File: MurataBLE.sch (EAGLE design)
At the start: 50 parts, among them CON1 C-2235, IC1 I-5448, IC3 74LVC1G00DBV, IC4 IC_MEMORY_8P_AT25XE011_SOP, IC5 IC_MEMORY_8P_AT25XE011_TSSOP, Q1 FC-135 32.7680KA-AG3, U1 LBCA2HNZYZ-711, X1 C-04397

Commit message: [ USB ] r0.4
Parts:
- added ICON1: r0.4, mylib:ICON_REVISION_1.2
- TR1: device mylib:TR_PMOS_GDS_SOT23 -> mylib:PMOS_BSS84_SOT23
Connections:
- net N$14 renamed P1_15
- net N$25 renamed P0_32
- net N$26 renamed P0_16
- net N$27 renamed P0_15
- net P0_2: now also IC2.P0_7/CTS
- net P0_3: now also IC2.P0_8/MISO0
- net P0_6: now also IC2.P0_9/MOSI0
- net P1_1: now also IC2.P0_21/MOSI1
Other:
- note removed: "rev 0.3"
- moved on the sheet: TP1, TP2, TP3, TP4, TP5, TP6, TP7, TP8
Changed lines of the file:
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@@
 <part name="SUPPLY14" library="mylib" deviceset="GND" device=""/>
 <part name="SUPPLY15" library="mylib" deviceset="GND" device=""/>
-<part name="TR1" library="mylib" deviceset="TR_PMOS_GDS" device="_SOT23" value="I-4269"/>
+<part name="TR1" library="mylib" deviceset="PMOS_*" device="_SOT23" technology="BSS84" value="I-4269"/>
 <part name="R10" library="mylib" deviceset="R_US_*" device="_1005" technology="1.5K" value="1.5k/1005"/>
 <part name="IC3" library="74xx-little-us_local" deviceset="74*1G00" device="DBV" technology="LVC" value="74LVC1G00DBV"/>
@@
 <part name="C11" library="mylib" deviceset="C_SMD_*" device="_1005" technology="0.1U" value="0.1u/1005"/>
 <part name="C12" library="mylib" deviceset="C_SMD_*" device="_1005" technology="0.1U" value="0.1u/1005"/>
+<part name="ICON1" library="mylib" deviceset="ICON_REVISION" device="_1.2" value="r0.4"/>
 </parts>
 <sheets>
 <sheet>
 <plain>
-<text x="162.56" y="5.08" size="5.08" layer="94">rev 0.3</text>
 <text x="190.5" y="96.52" size="1.778" layer="91">Vf@5mA:
 (R) = 1.9V
 (G) = 2.9V
 (B) = 2.8V</text>
-<text x="187.96" y="50.8" size="1.778" layer="94">TGT_TX &lt;- P0_0
+<text x="203.2" y="50.8" size="1.778" layer="94">TGT_TX &lt;- P0_0
 TGT_RX -&gt; P0_1</text>
 <text x="233.68" y="139.7" size="1.778" layer="94">P0_0 -&gt; TGT_TX
@@
 <instance part="LED1" gate="G" x="175.26" y="96.52" rot="R90"/>
 <instance part="LED1" gate="B" x="180.34" y="93.98" rot="R90"/>
-<instance part="TP5" gate="G$1" x="165.1" y="55.88"/>
-<instance part="TP6" gate="G$1" x="165.1" y="48.26" rot="R180"/>
-<instance part="TP7" gate="G$1" x="185.42" y="48.26" rot="R180"/>
-<instance part="TP8" gate="G$1" x="185.42" y="55.88"/>
+<instance part="TP5" gate="G$1" x="180.34" y="55.88"/>
+<instance part="TP6" gate="G$1" x="180.34" y="48.26" rot="R180"/>
+<instance part="TP7" gate="G$1" x="200.66" y="48.26" rot="R180"/>
+<instance part="TP8" gate="G$1" x="200.66" y="55.88"/>
 <instance part="X1" gate="-1" x="231.14" y="93.98" rot="MR0"/>
 <instance part="X1" gate="-2" x="231.14" y="91.44" rot="MR0"/>
@@
 <instance part="X1" gate="-13" x="231.14" y="63.5" rot="MR0"/>
 <instance part="X1" gate="-14" x="231.14" y="60.96" rot="MR0"/>
-<instance part="TP1" gate="1" x="167.64" y="53.34"/>
-<instance part="TP2" gate="1" x="167.64" y="50.8"/>
-<instance part="TP3" gate="1" x="182.88" y="53.34" rot="R180"/>
-<instance part="TP4" gate="1" x="182.88" y="50.8" rot="R180"/>
+<instance part="TP1" gate="1" x="182.88" y="53.34"/>
+<instance part="TP2" gate="1" x="182.88" y="50.8"/>
+<instance part="TP3" gate="1" x="198.12" y="53.34" rot="R180"/>
+<instance part="TP4" gate="1" x="198.12" y="50.8" rot="R180"/>
 <instance part="TP9" gate="1" x="144.78" y="15.24" rot="R90"/>
 <instance part="TP10" gate="1" x="149.86" y="15.24" rot="R90"/>
@@
 <instance part="C11" gate="G$1" x="48.26" y="68.58"/>
 <instance part="C12" gate="G$1" x="48.26" y="45.72"/>
+<instance part="ICON1" gate="G$1" x="162.56" y="5.08"/>
 </instances>
 <busses>
@@
 <label x="10.16" y="40.64" size="1.778" layer="95"/>
 </segment>
+<segment>
+<wire x1="170.18" y1="83.82" x2="157.48" y2="83.82" width="0.1524" layer="91"/>
+<pinref part="IC2" gate="G$1" pin="P0_9/MOSI0"/>
+<label x="170.18" y="83.82" size="1.778" layer="95"/>
+</segment>
 </net>
 <net name="P0_7" class="0">
@@
 <label x="48.26" y="35.56" size="1.778" layer="95"/>
 </segment>
+<segment>
+<wire x1="170.18" y1="88.9" x2="157.48" y2="88.9" width="0.1524" layer="91"/>
+<pinref part="IC2" gate="G$1" pin="P0_7/CTS"/>
+<label x="170.18" y="88.9" size="1.778" layer="95"/>
+</segment>
 </net>
 <net name="P0_3" class="0">
@@
 <label x="10.16" y="38.1" size="1.778" layer="95"/>
 </segment>
+<segment>
+<wire x1="170.18" y1="86.36" x2="157.48" y2="86.36" width="0.1524" layer="91"/>
+<pinref part="IC2" gate="G$1" pin="P0_8/MISO0"/>
+<label x="170.18" y="86.36" size="1.778" layer="95"/>
+</segment>
 </net>
 <net name="P0_4" class="0">
@@
 <pinref part="IC5" gate="G$1" pin="!CS"/>
 <label x="10.16" y="43.18" size="1.778" layer="95"/>
+</segment>
+<segment>
+<wire x1="170.18" y1="91.44" x2="157.48" y2="91.44" width="0.1524" layer="91"/>
+<pinref part="IC2" gate="G$1" pin="P0_21/MOSI1"/>
+<label x="170.18" y="91.44" size="1.778" layer="95"/>
 </segment>
 </net>
@@
 <segment>
 <pinref part="TP5" gate="G$1" pin="TP"/>
-<junction x="165.1" y="53.34"/>
+<junction x="180.34" y="53.34"/>
 <pinref part="TP1" gate="1" pin="1"/>
-<wire x1="193.04" y1="53.34" x2="185.42" y2="53.34" width="0.1524" layer="91"/>
+<wire x1="208.28" y1="53.34" x2="200.66" y2="53.34" width="0.1524" layer="91"/>
 <pinref part="TP8" gate="G$1" pin="TP"/>
-<junction x="185.42" y="53.34"/>
+<junction x="200.66" y="53.34"/>
 <pinref part="TP3" gate="1" pin="1"/>
-<wire x1="165.1" y1="53.34" x2="167.64" y2="55.88" width="0.1524" layer="91"/>
-<wire x1="167.64" y1="55.88" x2="182.88" y2="55.88" width="0.1524" layer="91"/>
-<wire x1="182.88" y1="55.88" x2="185.42" y2="53.34" width="0.1524" layer="91"/>
-<wire x1="157.48" y1="53.34" x2="165.1" y2="53.34" width="0.1524" layer="91"/>
+<wire x1="180.34" y1="53.34" x2="182.88" y2="55.88" width="0.1524" layer="91"/>
+<wire x1="182.88" y1="55.88" x2="198.12" y2="55.88" width="0.1524" layer="91"/>
+<wire x1="198.12" y1="55.88" x2="200.66" y2="53.34" width="0.1524" layer="91"/>
+<wire x1="157.48" y1="53.34" x2="180.34" y2="53.34" width="0.1524" layer="91"/>
 <pinref part="IC2" gate="G$1" pin="P0_18/RXD&lt;-"/>
 </segment>
@@
 <net name="TGT_RX" class="0">
 <segment>
-<wire x1="193.04" y1="50.8" x2="185.42" y2="50.8" width="0.1524" layer="91"/>
+<wire x1="208.28" y1="50.8" x2="200.66" y2="50.8" width="0.1524" layer="91"/>
 <pinref part="TP7" gate="G$1" pin="TP"/>
-<junction x="185.42" y="50.8"/>
+<junction x="200.66" y="50.8"/>
 <pinref part="TP4" gate="1" pin="1"/>
 <pinref part="TP6" gate="G$1" pin="TP"/>
-<junction x="165.1" y="50.8"/>
+<junction x="180.34" y="50.8"/>
 <pinref part="TP2" gate="1" pin="1"/>
-<wire x1="185.42" y1="50.8" x2="182.88" y2="48.26" width="0.1524" layer="91"/>
-<wire x1="182.88" y1="48.26" x2="167.64" y2="48.26" width="0.1524" layer="91"/>
-<wire x1="167.64" y1="48.26" x2="165.1" y2="50.8" width="0.1524" layer="91"/>
-<wire x1="157.48" y1="50.8" x2="165.1" y2="50.8" width="0.1524" layer="91"/>
+<wire x1="200.66" y1="50.8" x2="198.12" y2="48.26" width="0.1524" layer="91"/>
+<wire x1="198.12" y1="48.26" x2="182.88" y2="48.26" width="0.1524" layer="91"/>
+<wire x1="182.88" y1="48.26" x2="180.34" y2="50.8" width="0.1524" layer="91"/>
+<wire x1="157.48" y1="50.8" x2="180.34" y2="50.8" width="0.1524" layer="91"/>
 <pinref part="IC2" gate="G$1" pin="P0_19/TXD-&gt;"/>
 </segment>
@@
 </segment>
 </net>
-<net name="N$14" class="0">
+<net name="P1_15" class="0">
 <segment>
 <pinref part="IC2" gate="G$1" pin="P1_15"/>
 <wire x1="157.48" y1="58.42" x2="162.56" y2="58.42" width="0.1524" layer="91"/>
+<label x="162.56" y="58.42" size="1.778" layer="95"/>
 </segment>
 <segment>
@@
 </segment>
 </net>
-<net name="N$25" class="0">
+<net name="P0_32" class="0">
 <segment>
 <pinref part="IC2" gate="G$1" pin="P0_32/AD7"/>
 <wire x1="157.48" y1="60.96" x2="162.56" y2="60.96" width="0.1524" layer="91"/>
+<label x="162.56" y="60.96" size="1.778" layer="95"/>
 </segment>
 <segment>
@@
 </segment>
 </net>
-<net name="N$26" class="0">
+<net name="P0_16" class="0">
 <segment>
 <pinref part="IC2" gate="G$1" pin="P0_16/AD5"/>
 <wire x1="157.48" y1="63.5" x2="162.56" y2="63.5" width="0.1524" layer="91"/>
+<label x="162.56" y="63.5" size="1.778" layer="95"/>
 </segment>
 <segment>
@@
 </segment>
 </net>
-<net name="N$27" class="0">
+<net name="P0_15" class="0">
 <segment>
 <pinref part="IC2" gate="G$1" pin="P0_15/SWDIO/AD4"/>
 <wire x1="157.48" y1="66.04" x2="162.56" y2="66.04" width="0.1524" layer="91"/>
-</segment>
-<segment>
+<label x="162.56" y="66.04" size="1.778" layer="95"/>
+</segment>
+<segment>

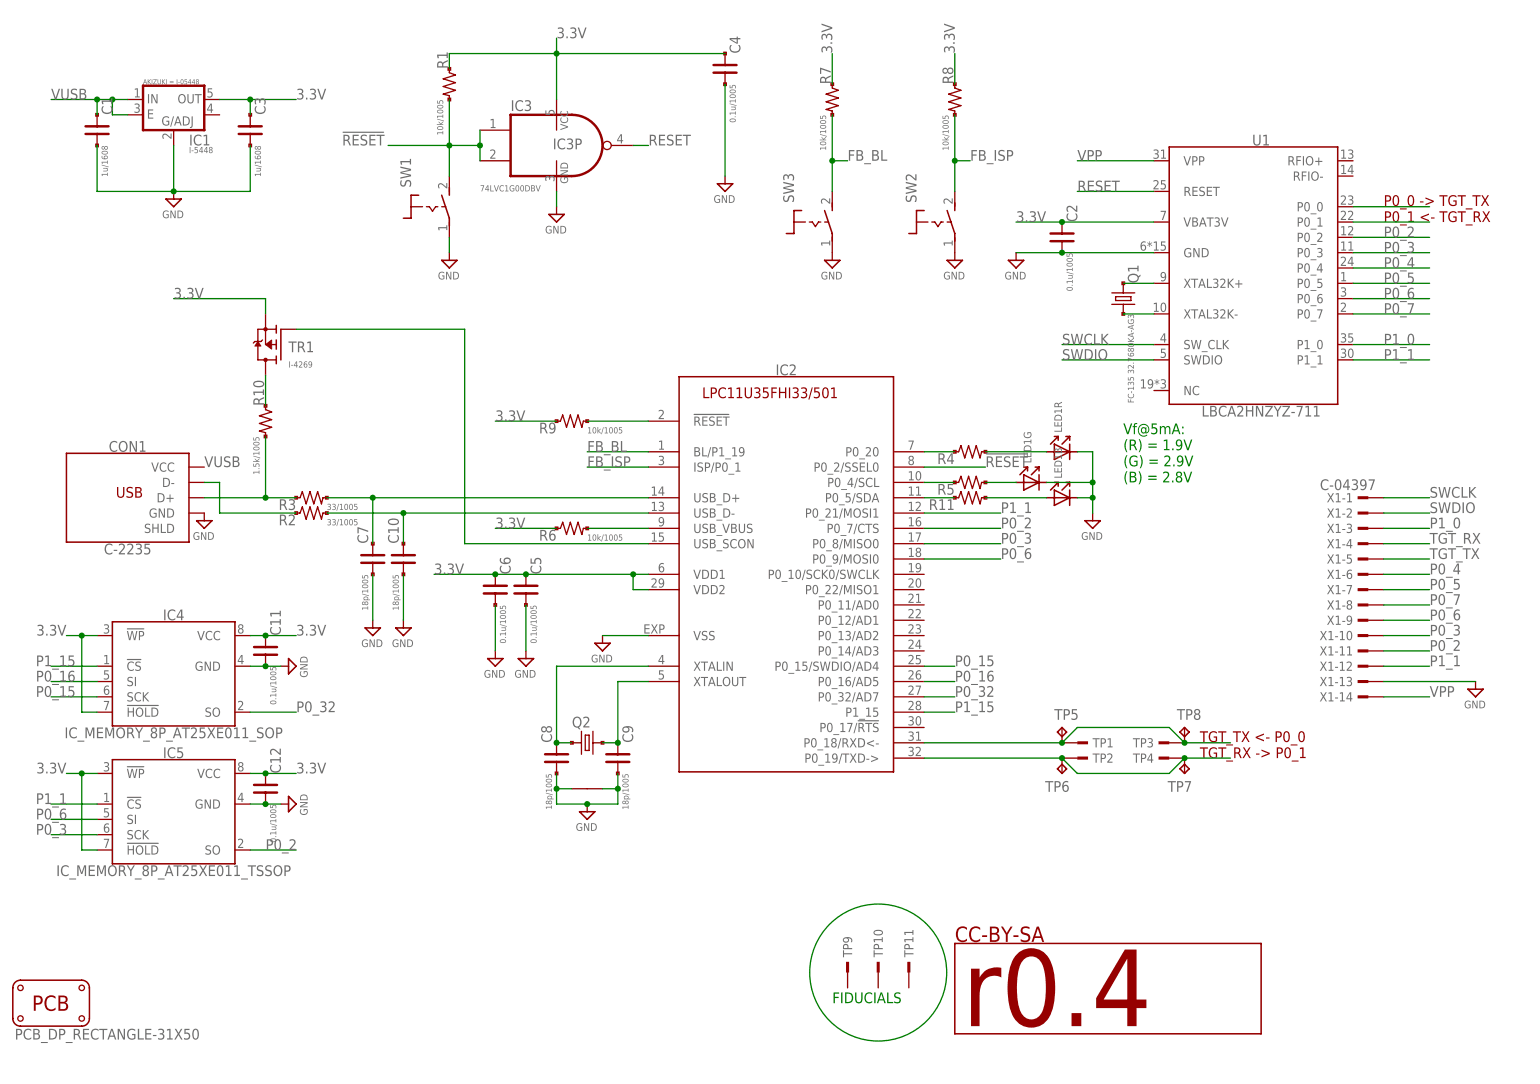
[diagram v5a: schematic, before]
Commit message: [ USB ] no more 580.P1_x use for SPI
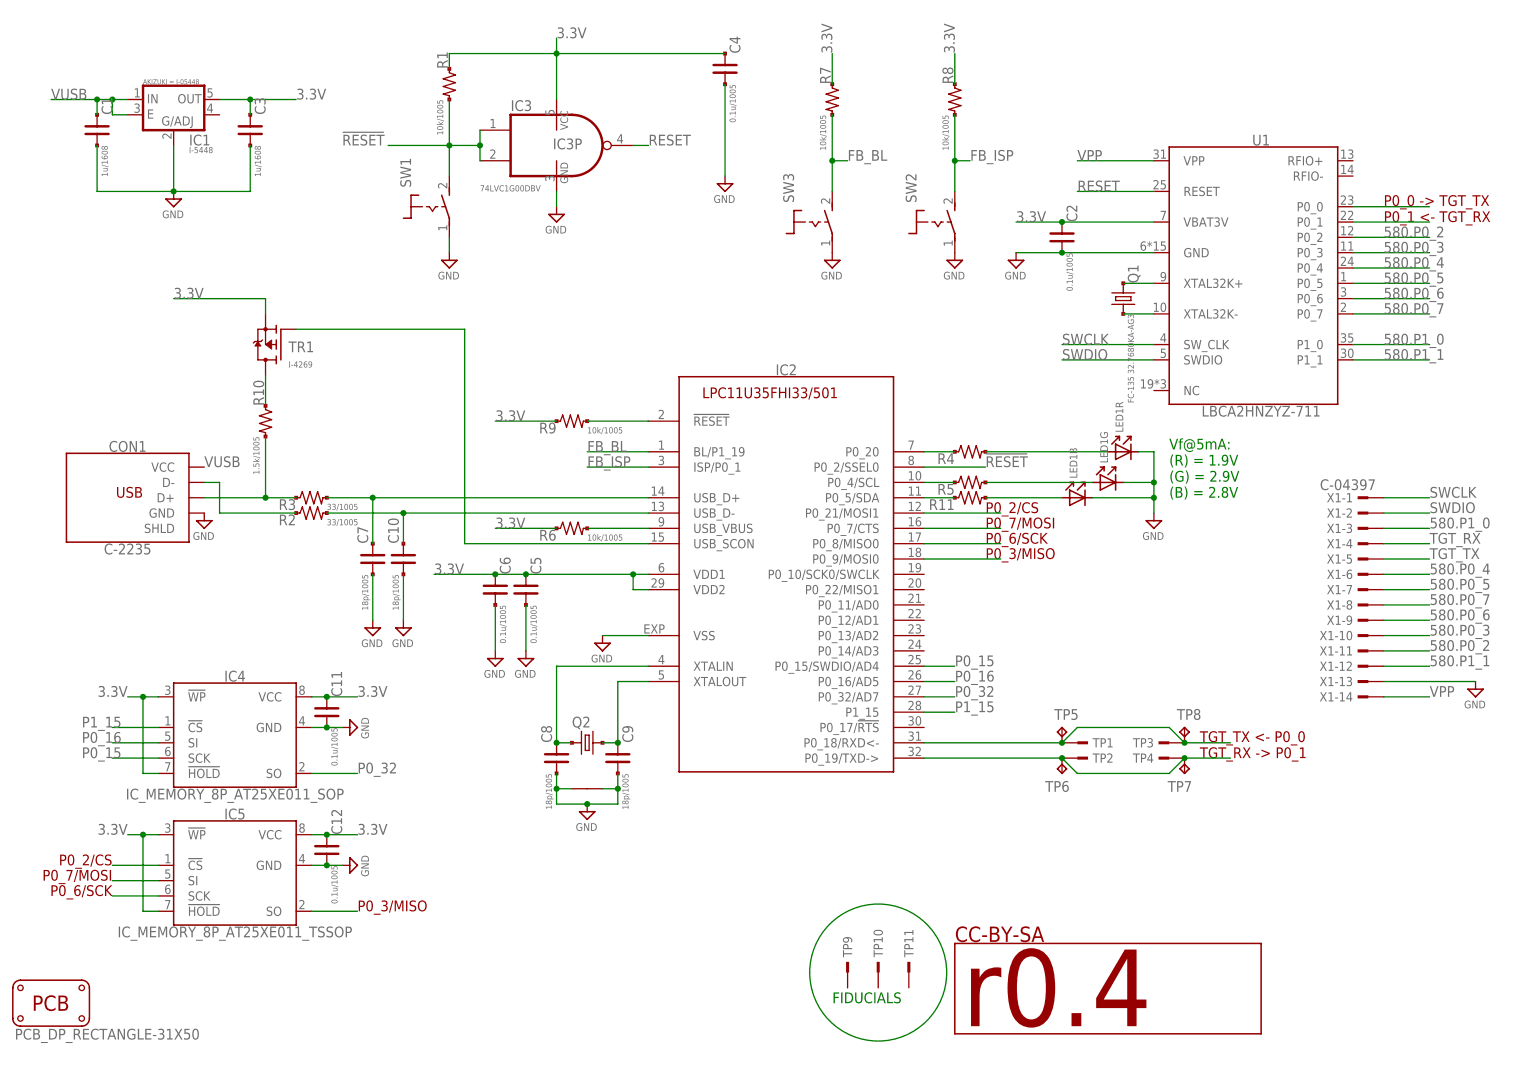
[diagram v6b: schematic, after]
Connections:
- net P0_4 renamed 580.P0_4
- net P0_5 renamed 580.P0_5
- net P1_0 renamed 580.P1_0
- removed net P0_2: IC2.P0_7/CTS, IC5.SO, U1.P0_2, X1-11.1
- removed net P0_3: IC2.P0_8/MISO0, IC5.SCK, U1.P0_3, X1-10.1
- removed net P0_6: IC2.P0_9/MOSI0, IC5.SI, U1.P0_6, X1-9.1
- removed net P0_7: U1.P0_7, X1-8.1
- removed net P1_1: IC2.P0_21/MOSI1, IC5.!CS, U1.P1_1, X1-12.1
- new net 580.P0_2: IC2.P0_21/MOSI1, IC5.!CS, U1.P0_2, X1-11.1
- new net 580.P0_3: IC2.P0_7/CTS, IC5.SO, U1.P0_3, X1-10.1
- new net 580.P0_6: IC2.P0_8/MISO0, IC5.SCK, U1.P0_6, X1-9.1
- new net 580.P0_7: IC2.P0_9/MOSI0, IC5.SI, U1.P0_7, X1-8.1
- new net 580.P1_1: U1.P1_1, X1-12.1
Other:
- note added: "P0_2/CS"
- note added: "P0_3/MISO"
- note added: "P0_6/SCK"
- note added: "P0_7/MOSI"
- moved on the sheet: C11, C12, IC4, IC5, LED1B, LED1G, LED1R

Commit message: [ USB ] OSHW; milling; CON1;
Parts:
- removed PCB1: PCB_DP_RECTANGLE-31X50, dp_pcb:PCB_DP_RECTANGLE-31X50
- removed TP10, TP11, TP9: TESTPAD_F, mylib:TESTPAD_F
- removed TP3, TP4: (no value), mylib:TESTPAD
- removed TP5, TP6, TP7, TP8: TPTP06R, testpad_local:TPTP06R
- added ICON2: (no value), mylib:ICON_OSHW
- added P1, P2, P3, P4: (no value), mylib:PCB_CORNER
- added TP100, TP101, TP102: TESTPAD_F, mylib:TESTPAD_F
- CON1: value C-2235 -> (none); device mylib:CON_USB_MINIB -> mylib:CON_USB_UB
- TP1, TP2: device mylib:TESTPAD -> mylib:TESTPAD_1608
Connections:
- net GND: now also CON1.SHLD
- net TGT_RX: no longer TP4.1, TP6.TP, TP7.TP
- net TGT_TX: no longer TP3.1, TP5.TP, TP8.TP
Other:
- moved on the sheet: TP1, TP2
